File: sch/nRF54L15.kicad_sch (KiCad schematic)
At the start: 20 parts, among them J6 Conn_01x05_MountingPin, SW1 SW_Push, SW2 SW_Push, U1 BM15x, U4 W25Q16JVUXIQ, Y1 32.768KHz

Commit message: Updated to include castellations, more testpoints
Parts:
- R2, R3: now not fitted; now left out of the parts list
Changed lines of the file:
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@@
 		(unit 1)
 		(exclude_from_sim no)
-		(in_bom yes)
-		(on_board yes)
-		(dnp no)
+		(in_bom no)
+		(on_board yes)
+		(dnp yes)
 		(property "Reference" "R3"
 			(at 233.68 96.5199 0)
@@
 		(unit 1)
 		(exclude_from_sim no)
-		(in_bom yes)
-		(on_board yes)
-		(dnp no)
+		(in_bom no)
+		(on_board yes)
+		(dnp yes)
 		(fields_autoplaced yes)
 		(property "Reference" "R2"

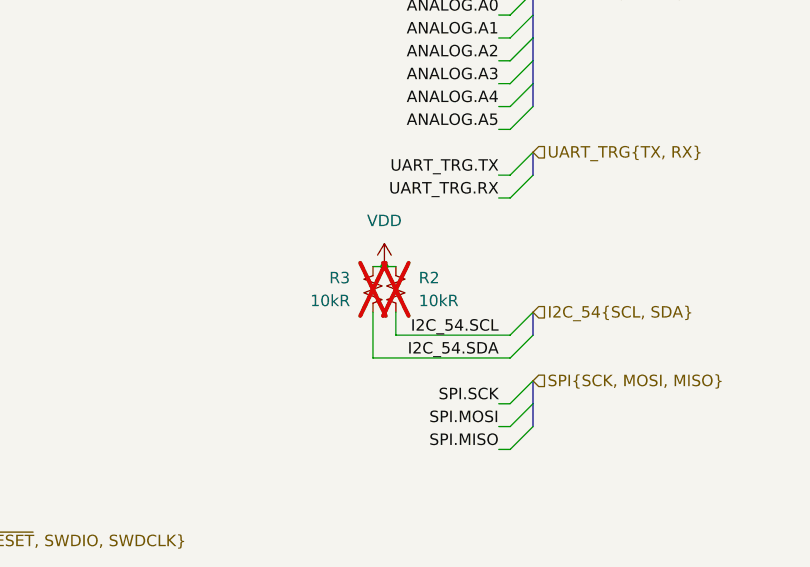
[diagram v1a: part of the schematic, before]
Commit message: Updated all vias to share size, fixed zone fill outlines
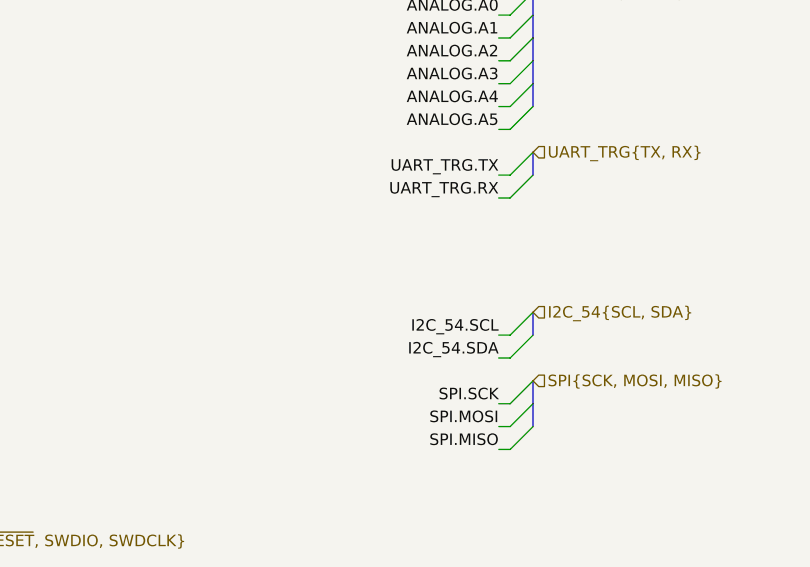
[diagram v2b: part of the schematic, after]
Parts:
- removed R2, R3: 10kR, Resistor_SMD:R_0402_1005Metric, symbol Device:R_Small_US

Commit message: Fixed DRC errors
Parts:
- J6: LCSC (none) -> C5213747
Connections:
- net ANALOG.A0: now also U1.F8 (P1.05/AIN1); no longer U1.E9 (P1.04/AIN0)
- net ANALOG.A1: now also U1.E9 (P1.04/AIN0); no longer U1.F8 (P1.05/AIN1)
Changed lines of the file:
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@@
 	)
 	(label "ANALOG.A1"
-		(at 116.84 69.85 180)
+		(at 116.84 67.31 180)
 		(effects
 			(font
@@
 	)
 	(label "ANALOG.A0"
-		(at 116.84 67.31 180)
+		(at 116.84 69.85 180)
 		(effects
 			(font
@@
 			)
 		)
-		(property "Description" "Generic connectable mounting pin connector, single row, 01x05, script generated (kicad-library-utils/schlib/autogen/connector/)"
+		(property "Description" "Generic connectable mounting pin connector, single row, 01x05"
 			(at 76.2 63.5 0)
 			(effects
+				(font
+					(size 1.27 1.27)
+				)
+				(hide yes)
+			)
+		)
+		(property "LCSC" "C5213747"
+			(at 76.2 63.5 0)
+			(effects
